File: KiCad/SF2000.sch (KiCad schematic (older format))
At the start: 74 parts, among them J1 Conn_2Rows-86Pins_even_odd, J2 Conn_01x02, J7 Conn_02x01, U1 LM1117-3.3, U19 74LVC1G57GV, U2 ABLIC S-1132B43-M5T1U, U3 TLV75533PDBVR, U4 SN74CBT16211, U5 SN74CBT16211, U6 SN74CBT3244PW, U7 SN74LVC16245ADGGR

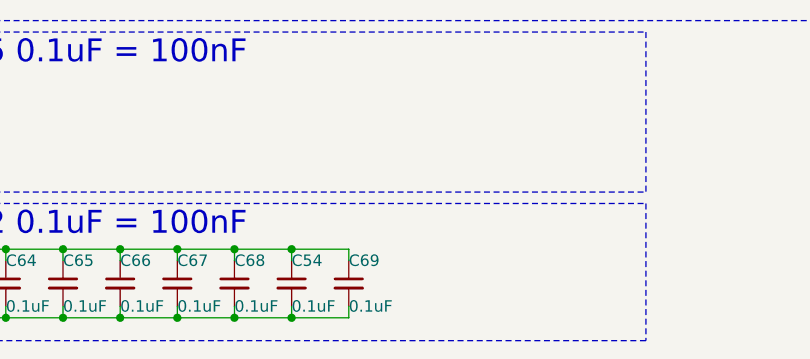
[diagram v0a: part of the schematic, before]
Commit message: Add capacitor C70 and place near P7,P9,N9 pads on FPGA.
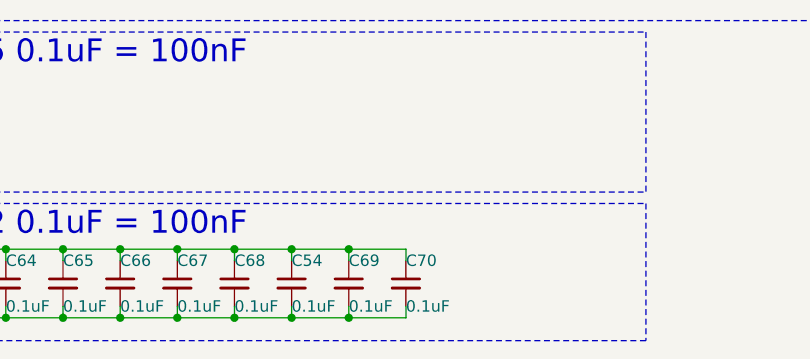
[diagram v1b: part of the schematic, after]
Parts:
- added C70: 0.1uF, Capacitor_SMD:C_0402_1005Metric_Pad0.74x0.62mm_HandSolder, symbol Device:C_Small
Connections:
- net 3V3: now also C70.2
- net GND: now also C70.1
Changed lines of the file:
@@
 	5500 7650 5500 7600
 Connection ~ 5250 7650
+$Comp
+L Device:C_Small C70
+U 1 1 6BBA2BDF
+P 5750 7500
+F 0 "C70" H 5750 7600 50  0000 L CNN
+F 1 "0.1uF" H 5750 7400 50  0000 L CNN
+F 2 "Capacitor_SMD:C_0402_1005Metric_Pad0.74x0.62mm_HandSolder" H 5750 7500 50  0001 C CNN
+F 3 "~" H 5750 7500 50  0001 C CNN
+	1    5750 7500
+	1    0    0    -1
+$EndComp
+Wire Wire Line
+	5500 7350 5750 7350
+Wire Wire Line
+	5750 7350 5750 7400
+Connection ~ 5500 7350
+Wire Wire Line
+	5500 7650 5750 7650
+Wire Wire Line
+	5750 7650 5750 7600
+Connection ~ 5500 7650
 $EndSCHEMATC

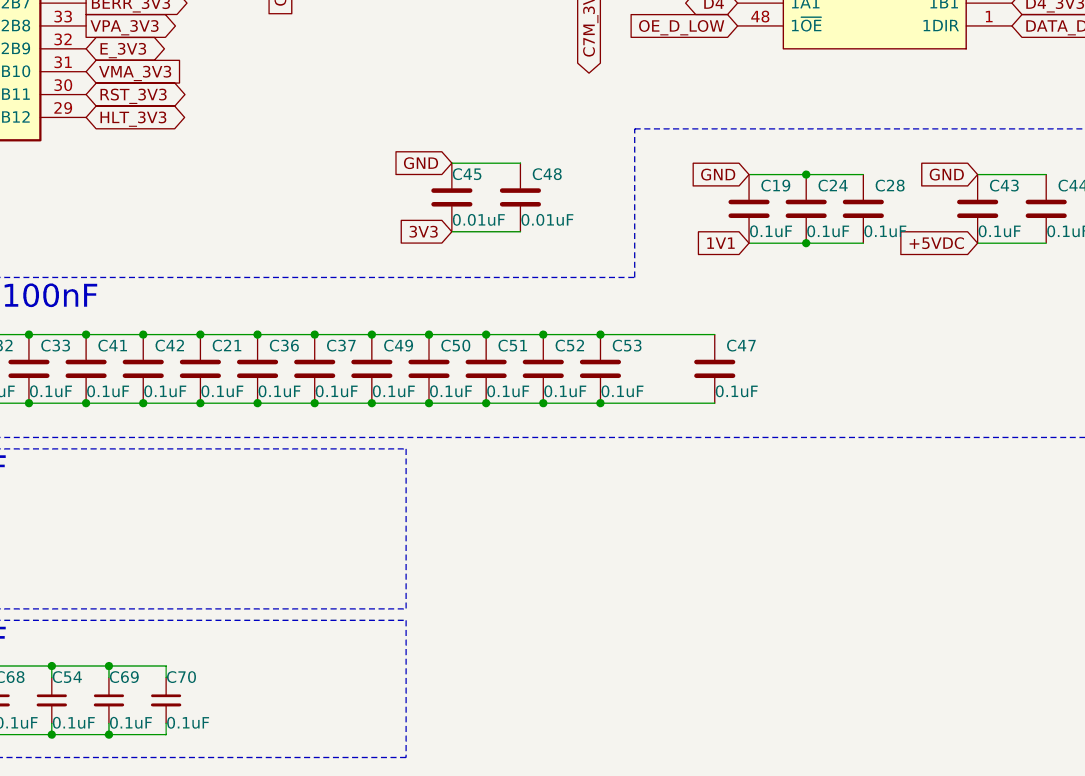
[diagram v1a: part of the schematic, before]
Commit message: Change C53 to size 0402
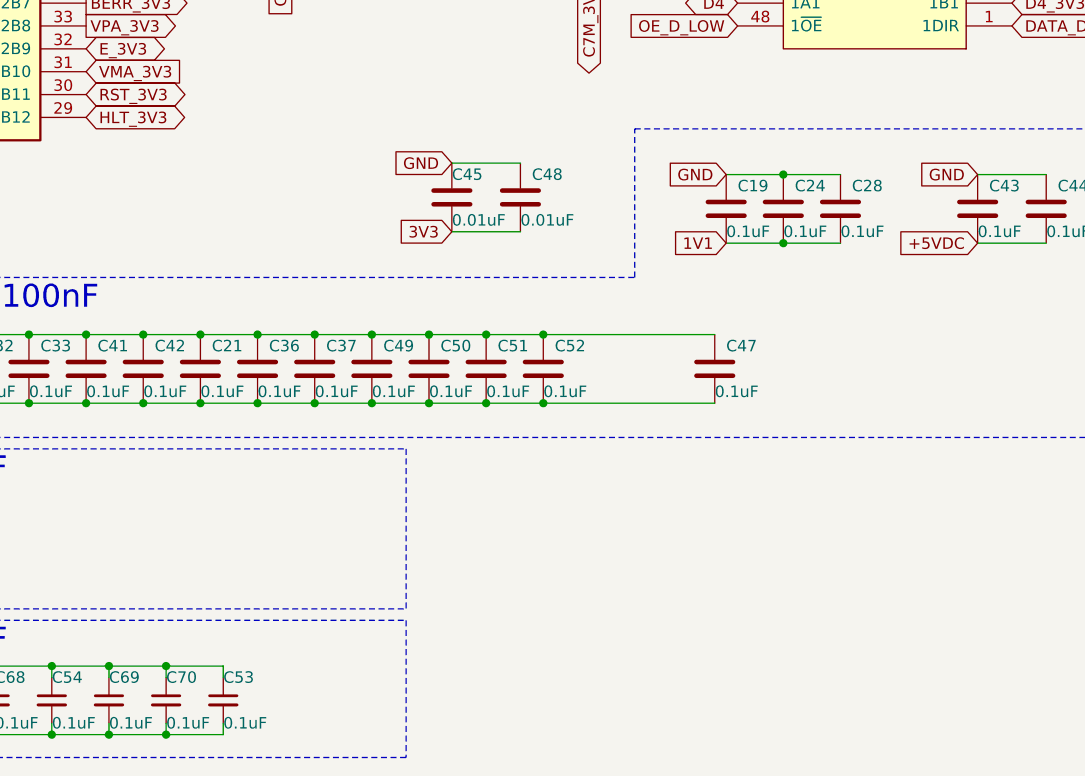
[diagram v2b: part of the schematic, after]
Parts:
- removed C53: 0.1uF, Capacitor_SMD:C_0603_1608Metric_Pad1.08x0.95mm_HandSolder, symbol Device:C
- added C53: 0.1uF, Capacitor_SMD:C_0402_1005Metric_Pad0.74x0.62mm_HandSolder, symbol Device:C_Small
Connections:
- net 3V3: now also C53.2
- net GND: now also C53.1
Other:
- moved on the sheet: C19, C24, C28
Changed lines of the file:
@@
-$EndComp
-$Comp
-L Device:C C53
-U 1 1 6231C987
-P 7650 6050
-F 0 "C53" H 7700 6150 50  0000 L CNN
-F 1 "0.1uF" H 7650 5950 50  0000 L CNN
-F 2 "Capacitor_SMD:C_0603_1608Metric_Pad1.08x0.95mm_HandSolder" H 7688 5900 50  0001 C CNN
-F 3 "~" H 7650 6050 50  0001 C CNN
-	1    7650 6050
-	1    0    0    -1
 $EndComp
 $Comp
@@
 L Device:C C19
 U 1 1 62524EDA
-P 8300 5350
-F 0 "C19" H 8350 5450 50  0000 L CNN
-F 1 "0.1uF" H 8300 5250 50  0000 L CNN
-F 2 "Capacitor_SMD:C_0603_1608Metric_Pad1.08x0.95mm_HandSolder" H 8338 5200 50  0001 C CNN
-F 3 "~" H 8300 5350 50  0001 C CNN
-	1    8300 5350
+P 8200 5350
+F 0 "C19" H 8250 5450 50  0000 L CNN
+F 1 "0.1uF" H 8200 5250 50  0000 L CNN
+F 2 "Capacitor_SMD:C_0603_1608Metric_Pad1.08x0.95mm_HandSolder" H 8238 5200 50  0001 C CNN
+F 3 "~" H 8200 5350 50  0001 C CNN
+	1    8200 5350
 	1    0    0    -1
 $EndComp
@@
 L Device:C C28
 U 1 1 6255AB6E
-P 8800 5350
-F 0 "C28" H 8850 5450 50  0000 L CNN
-F 1 "0.1uF" H 8800 5250 50  0000 L CNN
-F 2 "Capacitor_SMD:C_0603_1608Metric_Pad1.08x0.95mm_HandSolder" H 8838 5200 50  0001 C CNN
-F 3 "~" H 8800 5350 50  0001 C CNN
-	1    8800 5350
+P 8700 5350
+F 0 "C28" H 8750 5450 50  0000 L CNN
+F 1 "0.1uF" H 8700 5250 50  0000 L CNN
+F 2 "Capacitor_SMD:C_0603_1608Metric_Pad1.08x0.95mm_HandSolder" H 8738 5200 50  0001 C CNN
+F 3 "~" H 8700 5350 50  0001 C CNN
+	1    8700 5350
 	1    0    0    -1
 $EndComp
@@
 L Device:C C24
 U 1 1 6226DADA
-P 8550 5350
-F 0 "C24" H 8600 5450 50  0000 L CNN
-F 1 "0.1uF" H 8550 5250 50  0000 L CNN
-F 2 "Capacitor_SMD:C_0603_1608Metric_Pad1.08x0.95mm_HandSolder" H 8588 5200 50  0001 C CNN
-F 3 "~" H 8550 5350 50  0001 C CNN
-	1    8550 5350
+P 8450 5350
+F 0 "C24" H 8500 5450 50  0000 L CNN
+F 1 "0.1uF" H 8450 5250 50  0000 L CNN
+F 2 "Capacitor_SMD:C_0603_1608Metric_Pad1.08x0.95mm_HandSolder" H 8488 5200 50  0001 C CNN
+F 3 "~" H 8450 5350 50  0001 C CNN
+	1    8450 5350
 	1    0    0    -1
 $EndComp
@@
 Text Notes 4050 5800 0    100  ~ 0
 0603 0.1uF = 100nF
-Text GLabel 8300 5200 0    50   Input ~ 0
+Text GLabel 8200 5200 0    50   Input ~ 0
 GND
 Text GLabel 9300 5200 0    50   Input ~ 0
@@
 	2400 6200 2650 6200
 Wire Wire Line
-	8300 5200 8550 5200
-Wire Wire Line
-	8300 5500 8550 5500
-Text GLabel 8300 5500 0    50   Input ~ 0
+	8200 5200 8450 5200
+Wire Wire Line
+	8200 5500 8450 5500
+Text GLabel 8200 5500 0    50   Input ~ 0
 1V1
 Wire Wire Line
@@
 Wire Wire Line
 	3400 6200 3650 6200
-Connection ~ 8550 5200
-Wire Wire Line
-	8550 5200 8800 5200
-Connection ~ 8550 5500
-Wire Wire Line
-	8550 5500 8800 5500
+Connection ~ 8450 5200
+Wire Wire Line
+	8450 5200 8700 5200
+Connection ~ 8450 5500
+Wire Wire Line
+	8450 5500 8700 5500
 Connection ~ 3650 5900
 Connection ~ 3650 6200
@@
 	7400 6200 7150 6200
 Connection ~ 7150 6200
-Wire Wire Line
-	7650 5900 7400 5900
 Connection ~ 7400 5900
-Wire Wire Line
-	7650 6200 7400 6200
 Connection ~ 7400 6200
-Connection ~ 7650 5900
-Connection ~ 7650 6200
 Wire Notes Line
 	1850 5650 7800 5650
@@
 	5250 7650 5250 7600
 Connection ~ 5000 7650
-Wire Wire Line
-	7650 5900 8150 5900
-Wire Wire Line
-	7650 6200 8150 6200
 $Comp
 L Device:C_Small C69
@@
 	5750 7650 5750 7600
 Connection ~ 5500 7650
+$Comp
+L Device:C_Small C53
+U 1 1 6BBCB8BC
+P 6000 7500
+F 0 "C53" H 6000 7600 50  0000 L CNN
+F 1 "0.1uF" H 6000 7400 50  0000 L CNN
+F 2 "Capacitor_SMD:C_0402_1005Metric_Pad0.74x0.62mm_HandSolder" H 6000 7500 50  0001 C CNN
+F 3 "~" H 6000 7500 50  0001 C CNN
+	1    6000 7500
+	1    0    0    -1
+$EndComp
+Wire Wire Line
+	5750 7350 6000 7350
+Wire Wire Line
+	6000 7350 6000 7400
+Connection ~ 5750 7350
+Wire Wire Line
+	5750 7650 6000 7650
+Wire Wire Line
+	6000 7650 6000 7600
+Connection ~ 5750 7650
+Wire Wire Line
+	7400 5900 8150 5900
+Wire Wire Line
+	7400 6200 8150 6200
 $EndSCHEMATC

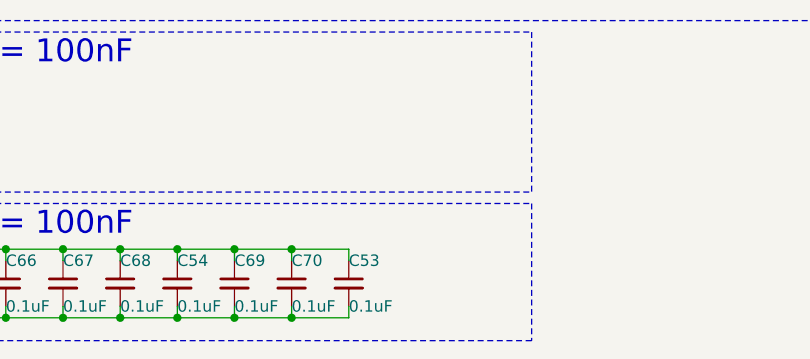
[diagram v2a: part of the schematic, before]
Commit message: Add capacitor C71 and place near E11,D11 pads on FPGA.
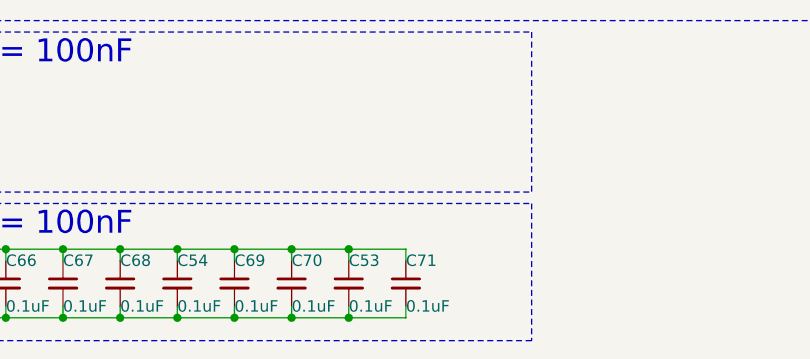
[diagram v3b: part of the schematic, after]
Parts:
- added C71: 0.1uF, Capacitor_SMD:C_0402_1005Metric_Pad0.74x0.62mm_HandSolder, symbol Device:C_Small
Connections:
- net 3V3: now also C71.2
- net GND: now also C71.1
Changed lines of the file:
@@
 Wire Wire Line
 	7400 6200 8150 6200
+$Comp
+L Device:C_Small C71
+U 1 1 6BC27B4F
+P 6250 7500
+F 0 "C71" H 6250 7600 50  0000 L CNN
+F 1 "0.1uF" H 6250 7400 50  0000 L CNN
+F 2 "Capacitor_SMD:C_0402_1005Metric_Pad0.74x0.62mm_HandSolder" H 6250 7500 50  0001 C CNN
+F 3 "~" H 6250 7500 50  0001 C CNN
+	1    6250 7500
+	1    0    0    -1
+$EndComp
+Wire Wire Line
+	6250 7400 6250 7350
+Wire Wire Line
+	6250 7350 6000 7350
+Connection ~ 6000 7350
+Wire Wire Line
+	6000 7650 6250 7650
+Wire Wire Line
+	6250 7650 6250 7600
+Connection ~ 6000 7650
 $EndSCHEMATC

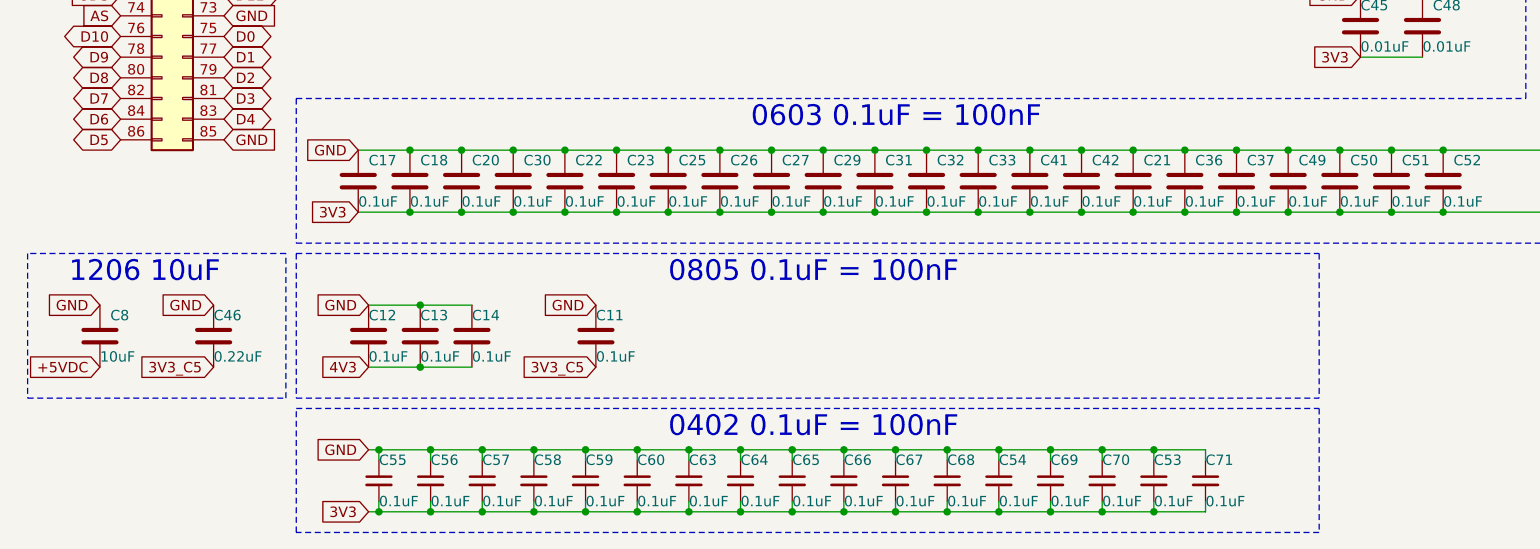
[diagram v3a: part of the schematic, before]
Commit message: Change C50 to size 0402
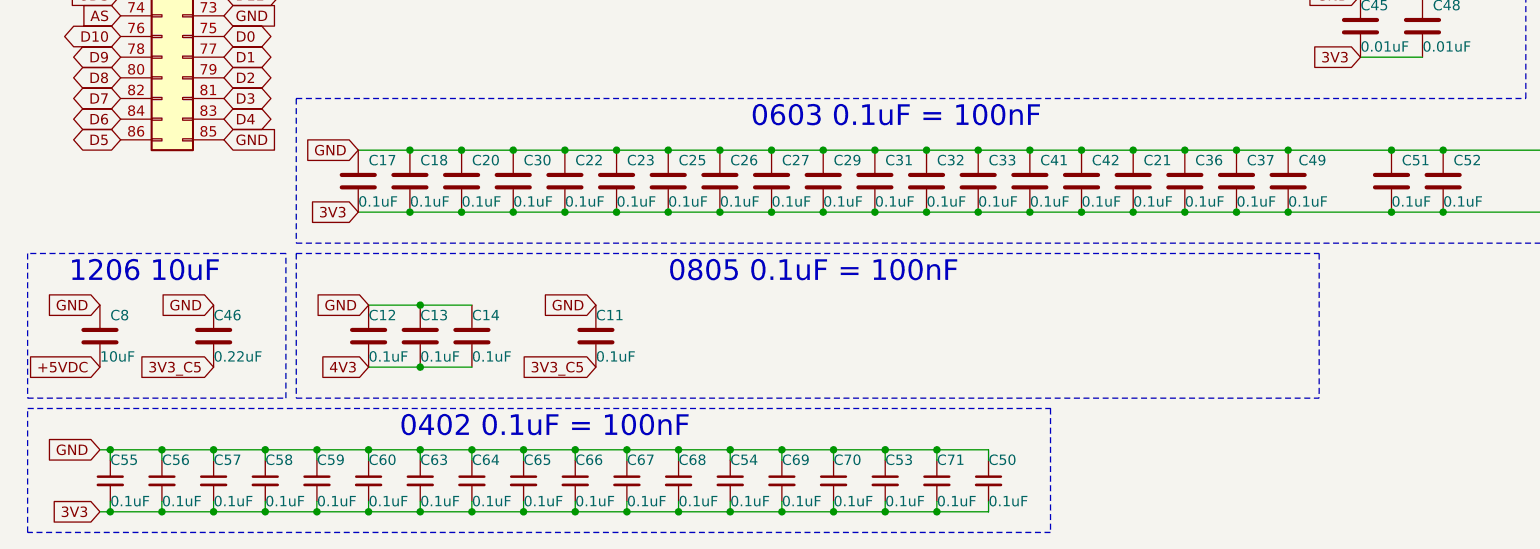
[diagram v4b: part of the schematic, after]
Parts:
- removed C50: 0.1uF, Capacitor_SMD:C_0603_1608Metric_Pad1.08x0.95mm_HandSolder, symbol Device:C
- added C50: 0.1uF, Capacitor_SMD:C_0402_1005Metric_Pad0.74x0.62mm_HandSolder, symbol Device:C_Small
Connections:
- net 3V3: now also C50.2
- net GND: now also C50.1
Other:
- moved on the sheet: C53, C54, C55, C56, C57, C58, C59, C60, C63, C64, C65, C66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

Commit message: Change C51 to size 0402
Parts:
- removed C51: 0.1uF, Capacitor_SMD:C_0603_1608Metric_Pad1.08x0.95mm_HandSolder, symbol Device:C
- added C51: 0.1uF, Capacitor_SMD:C_0402_1005Metric_Pad0.74x0.62mm_HandSolder, symbol Device:C_Small
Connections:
- net 3V3: now also C51.2
- net GND: now also C51.1
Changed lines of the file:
@@
-$EndComp
-$Comp
-L Device:C C51
-U 1 1 623684AD
-P 7150 6050
-F 0 "C51" H 7200 6150 50  0000 L CNN
-F 1 "0.1uF" H 7150 5950 50  0000 L CNN
-F 2 "Capacitor_SMD:C_0603_1608Metric_Pad1.08x0.95mm_HandSolder" H 7188 5900 50  0001 C CNN
-F 3 "~" H 7150 6050 50  0001 C CNN
-	1    7150 6050
-	1    0    0    -1
 $EndComp
 $Comp
@@
 Wire Notes Line
 	1850 6350 10000 6350
-Wire Wire Line
-	7400 5900 7150 5900
-Connection ~ 7150 5900
-Wire Wire Line
-	7400 6200 7150 6200
-Connection ~ 7150 6200
 Connection ~ 7400 5900
 Connection ~ 7400 6200
@@
 $EndComp
 Wire Notes Line
-	550  7150 5500 7150
-Wire Notes Line
-	5500 7150 5500 7750
-Wire Notes Line
-	5500 7750 550  7750
+	6800 7150 6800 7750
 Wire Notes Line
 	550  7750 550  7150
@@
 	5200 7650 4950 7650
 Connection ~ 4950 7650
-Wire Wire Line
-	6650 5900 7150 5900
-Wire Wire Line
-	6650 6200 7150 6200
+Wire Notes Line
+	550  7150 6800 7150
+Wire Notes Line
+	550  7750 6800 7750
+$Comp
+L Device:C_Small C51
+U 1 1 6BCECA9F
+P 5450 7500
+F 0 "C51" H 5450 7600 50  0000 L CNN
+F 1 "0.1uF" H 5450 7400 50  0000 L CNN
+F 2 "Capacitor_SMD:C_0402_1005Metric_Pad0.74x0.62mm_HandSolder" H 5450 7500 50  0001 C CNN
+F 3 "~" H 5450 7500 50  0001 C CNN
+	1    5450 7500
+	1    0    0    -1
+$EndComp
+Wire Wire Line
+	6650 5900 7400 5900
+Wire Wire Line
+	6650 6200 7400 6200
+Wire Wire Line
+	5200 7350 5450 7350
+Wire Wire Line
+	5450 7350 5450 7400
+Connection ~ 5200 7350
+Wire Wire Line
+	5200 7650 5450 7650
+Wire Wire Line
+	5450 7650 5450 7600
+Connection ~ 5200 7650
 $EndSCHEMATC

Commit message: Change C52 to size 0402
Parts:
- removed C52: 0.1uF, Capacitor_SMD:C_0603_1608Metric_Pad1.08x0.95mm_HandSolder, symbol Device:C
- added C52: 0.1uF, Capacitor_SMD:C_0402_1005Metric_Pad0.74x0.62mm_HandSolder, symbol Device:C_Small
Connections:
- net 3V3: now also C52.2
- net GND: now also C52.1
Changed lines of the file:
@@
-$EndComp
-$Comp
-L Device:C C52
-U 1 1 623684B7
-P 7400 6050
-F 0 "C52" H 7450 6150 50  0000 L CNN
-F 1 "0.1uF" H 7400 5950 50  0000 L CNN
-F 2 "Capacitor_SMD:C_0603_1608Metric_Pad1.08x0.95mm_HandSolder" H 7438 5900 50  0001 C CNN
-F 3 "~" H 7400 6050 50  0001 C CNN
-	1    7400 6050
-	1    0    0    -1
 $EndComp
 $Comp
@@
 Wire Notes Line
 	1850 6350 10000 6350
-Connection ~ 7400 5900
-Connection ~ 7400 6200
 Wire Notes Line
 	1850 5650 7800 5650
@@
 	4700 7650 4700 7600
 Connection ~ 4450 7650
-Wire Wire Line
-	7400 5900 8150 5900
-Wire Wire Line
-	7400 6200 8150 6200
 $Comp
 L Device:C_Small C71
@@
 $EndComp
 Wire Wire Line
-	6650 5900 7400 5900
-Wire Wire Line
-	6650 6200 7400 6200
-Wire Wire Line
 	5200 7350 5450 7350
 Wire Wire Line
@@
 	5450 7650 5450 7600
 Connection ~ 5200 7650
+$Comp
+L Device:C_Small C52
+U 1 1 6BD2050D
+P 5700 7500
+F 0 "C52" H 5700 7600 50  0000 L CNN
+F 1 "0.1uF" H 5700 7400 50  0000 L CNN
+F 2 "Capacitor_SMD:C_0402_1005Metric_Pad0.74x0.62mm_HandSolder" H 5700 7500 50  0001 C CNN
+F 3 "~" H 5700 7500 50  0001 C CNN
+	1    5700 7500
+	1    0    0    -1
+$EndComp
+Wire Wire Line
+	5450 7350 5700 7350
+Wire Wire Line
+	5700 7350 5700 7400
+Connection ~ 5450 7350
+Wire Wire Line
+	5450 7650 5700 7650
+Wire Wire Line
+	5700 7650 5700 7600
+Connection ~ 5450 7650
+Wire Wire Line
+	6650 5900 8150 5900
+Wire Wire Line
+	6650 6200 8150 6200
 $EndSCHEMATC

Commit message: Change C49 to size 0402
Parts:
- removed C49: 0.1uF, Capacitor_SMD:C_0603_1608Metric_Pad1.08x0.95mm_HandSolder, symbol Device:C
- added C49: 0.1uF, Capacitor_SMD:C_0402_1005Metric_Pad0.74x0.62mm_HandSolder, symbol Device:C_Small
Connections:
- net 3V3: now also C49.2
- net GND: now also C49.1
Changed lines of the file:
@@
 0805 0.1uF = 100nF
-$Comp
-L Device:C C49
-U 1 1 623192DF
-P 6650 6050
-F 0 "C49" H 6700 6150 50  0000 L CNN
-F 1 "0.1uF" H 6650 5950 50  0000 L CNN
-F 2 "Capacitor_SMD:C_0603_1608Metric_Pad1.08x0.95mm_HandSolder" H 6688 5900 50  0001 C CNN
-F 3 "~" H 6650 6050 50  0001 C CNN
-	1    6650 6050
-	1    0    0    -1
-$EndComp
 $Comp
 L Device:C C23
@@
 Connection ~ 6400 5900
 Connection ~ 6400 6200
-Wire Wire Line
-	6400 5900 6650 5900
-Wire Wire Line
-	6400 6200 6650 6200
-Connection ~ 6650 5900
-Connection ~ 6650 6200
 Wire Notes Line
 	1850 6350 10000 6350
@@
 	5700 7650 5700 7600
 Connection ~ 5450 7650
-Wire Wire Line
-	6650 5900 8150 5900
-Wire Wire Line
-	6650 6200 8150 6200
+$Comp
+L Device:C_Small C49
+U 1 1 6BD6E086
+P 5950 7500
+F 0 "C49" H 5950 7600 50  0000 L CNN
+F 1 "0.1uF" H 5950 7400 50  0000 L CNN
+F 2 "Capacitor_SMD:C_0402_1005Metric_Pad0.74x0.62mm_HandSolder" H 5950 7500 50  0001 C CNN
+F 3 "~" H 5950 7500 50  0001 C CNN
+	1    5950 7500
+	1    0    0    -1
+$EndComp
+Wire Wire Line
+	5700 7350 5950 7350
+Wire Wire Line
+	5950 7350 5950 7400
+Connection ~ 5700 7350
+Wire Wire Line
+	5700 7650 5950 7650
+Wire Wire Line
+	5950 7650 5950 7600
+Connection ~ 5700 7650
+Wire Wire Line
+	6400 5900 8150 5900
+Wire Wire Line
+	6400 6200 8150 6200
 $EndSCHEMATC

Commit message: Add capacitor C72 and place near C3 pad on FPGA.
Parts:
- added C72: 0.1uF, Capacitor_SMD:C_0402_1005Metric_Pad0.74x0.62mm_HandSolder, symbol Device:C_Small
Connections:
- net 3V3: now also C72.2
- net GND: now also C72.1
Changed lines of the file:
@@
 Wire Wire Line
 	6400 6200 8150 6200
+$Comp
+L Device:C_Small C72
+U 1 1 6BDA850E
+P 6200 7500
+F 0 "C72" H 6200 7600 50  0000 L CNN
+F 1 "0.1uF" H 6200 7400 50  0000 L CNN
+F 2 "Capacitor_SMD:C_0402_1005Metric_Pad0.74x0.62mm_HandSolder" H 6200 7500 50  0001 C CNN
+F 3 "~" H 6200 7500 50  0001 C CNN
+	1    6200 7500
+	1    0    0    -1
+$EndComp
+Wire Wire Line
+	6200 7400 6200 7350
+Wire Wire Line
+	6200 7350 5950 7350
+Connection ~ 5950 7350
+Wire Wire Line
+	6200 7600 6200 7650
+Wire Wire Line
+	6200 7650 5950 7650
+Connection ~ 5950 7650
 $EndSCHEMATC
